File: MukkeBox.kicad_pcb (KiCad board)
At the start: 2 copper layers, 200 x 105 mm, 278 parts, among them J101 Conn_02x20_Odd_Even, J102 Conn_01x04, J103 Conn_02x05_Odd_Even, J104 Conn_02x05_Odd_Even, J301 Conn_02x04_Odd_Even, J302 Conn_02x04_Odd_Even, J303 TB001-500-04BE CUI_Devices, J401 TB001-500-02BE CUI_Devices, J501 TB001-500-04BE CUI_Devices, J601 Conn_01x03_Female, J602 Conn_02x01, J603 Conn_02x06_Odd_Even, J604 Conn_02x01, J605 Conn_02x01, Q1 2N7002, Q201 VS6412AE, Q301 2N7002, Q302 HSBB3103, Q303 2N7002, Q304 HSBB3103, Q305 VS6412AE, Q306 2N7002, Q307 BSS84, Q308 2N7002, Q309 VS6412AE, Q310 HSBB3103, Q311 HSBB3103, Q501 2N7002, SW501 DS04-254-2-02BK-SMT, U101 LM35-LP, U102 STM32F030C6Tx_MukkeBox, U103 MCP9700, U202 StepUp, U203 TPS40210, U301 BQ24610, U501 TDA7498L, U502 BK8000L, U503 TDA7719, U504 AP2553AW6-7, U505 JW5026, U602 JW5026, Y101 FOXSDLF/080-20

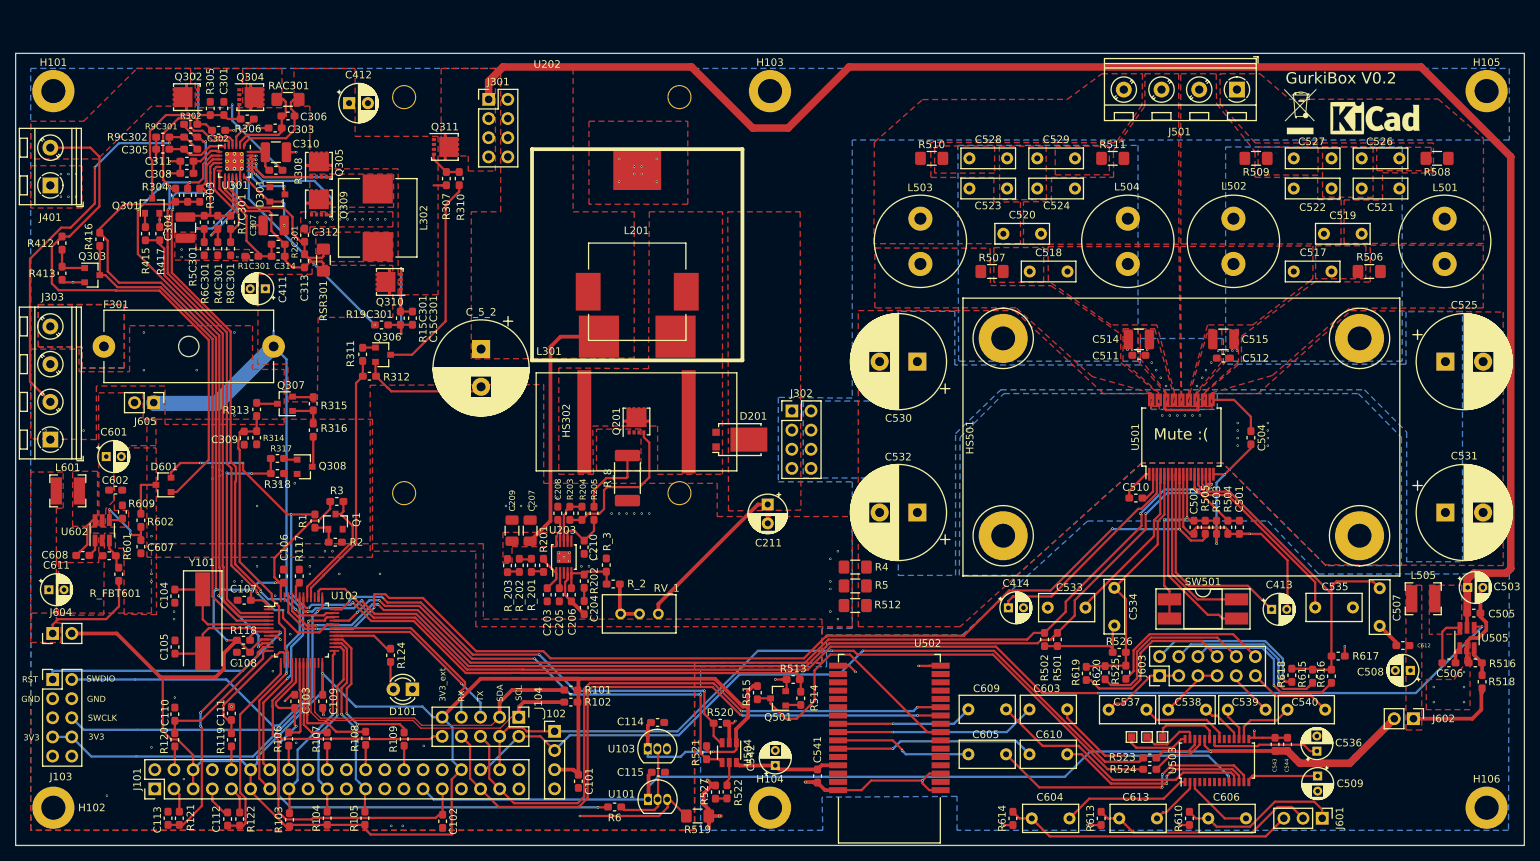
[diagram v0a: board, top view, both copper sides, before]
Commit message: Fehler bei Bestellung behoben: größere Vias. Platinen erfolgreich erhalten
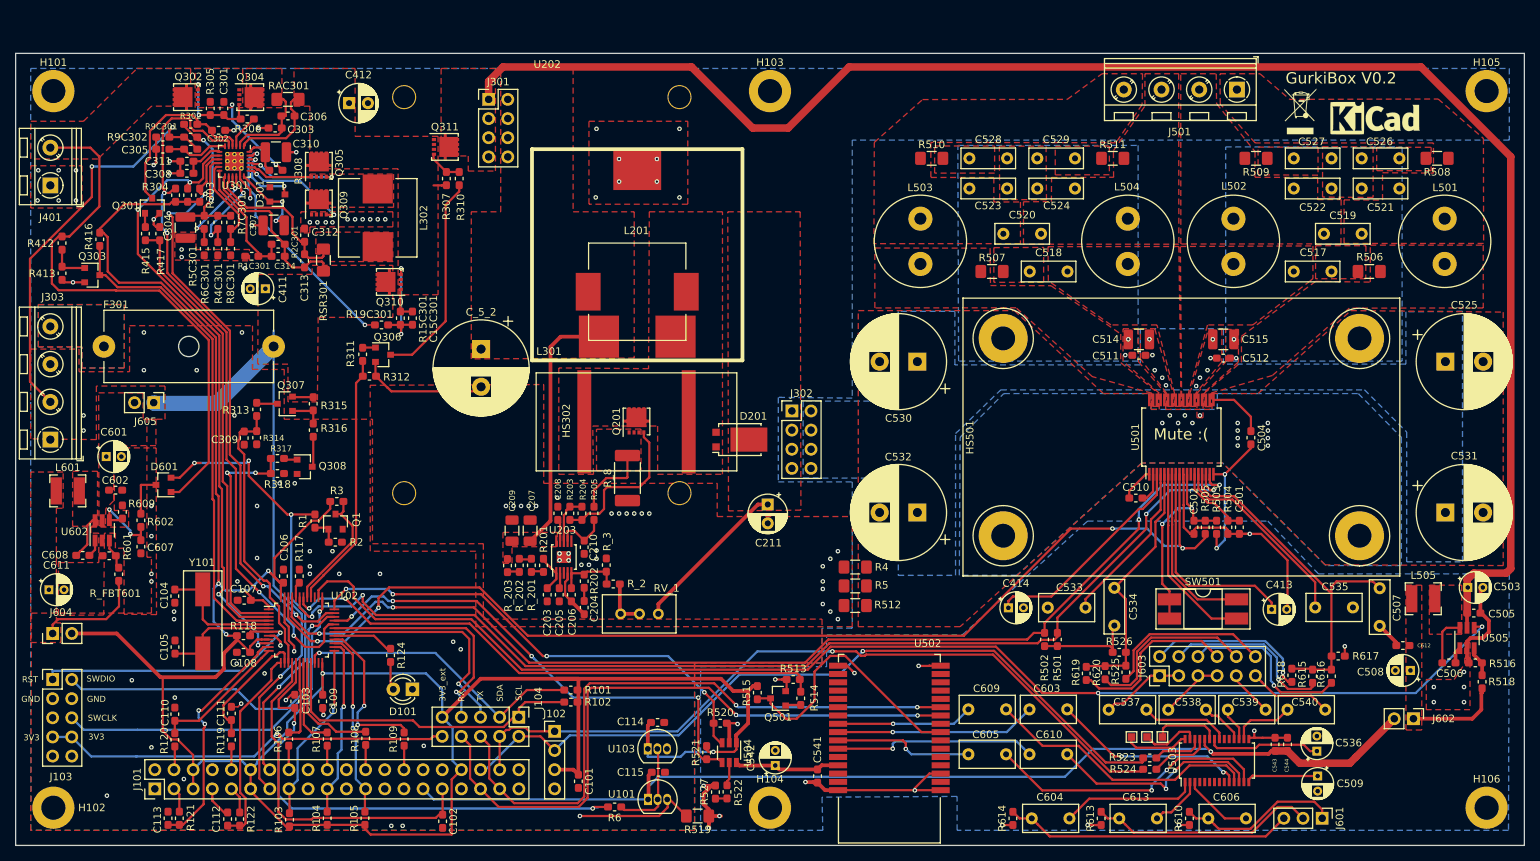
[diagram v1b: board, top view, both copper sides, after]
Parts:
- moved R118 0.60 mm to (75.7, 114.3)
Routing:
- net GND: track 61.8 -> 75.4 mm
- net GNDPWR: track 7.14 -> 0.00 mm, vias 20 -> 18
- net /UART1_RX: track 25.3 -> 31.2 mm
- net /UART1_TX: track 25.2 -> 30.4 mm
- net /I2C1_SDA: track 43.5 -> 39.2 mm, vias 0 -> 1
- net STBY_TDA7498: track 142.1 -> 146.3 mm
- net CHARGER_STAT1: track 92.5 -> 96.3 mm
- net +3V3: track 351.1 -> 354.5 mm
- net DIAG_TDA7498: track 146.6 -> 150.0 mm
- net /SWDIO: track 49.3 -> 46.0 mm
- net MUTE_TDA7498: track 140.8 -> 144.0 mm
- net Net-(C610-Pad2): track 27.0 -> 28.6 mm
- net /00_Charger/VREF: track 25.0 -> 26.6 mm
- net /00_Charger/TS: track 53.2 -> 54.7 mm
- net 3V3_EN: track 60.7 -> 62.2 mm
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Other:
- net class Default: trace_width 0.15 -> 0.2; via_dia 0.3 -> 0.6; via_drill 0.2 -> 0.3
- rule trace_min: 0.15 -> 0.2
- rule via_min_drill: 0.2 -> 0.3
- rule via_min_size: 0.3 -> 0.6

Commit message: Bereit zur Bestellung
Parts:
- removed C102, C115, C501, C502, C504, C510, C511: 100n, Capacitor_SMD:C_0603_1608Metric_Pad1.05x0.95mm_HandSolder
- removed C413, C414: 10u, Capacitor_THT:CP_Radial_D4.0mm_P2.00mm
- removed C514, C515: 2.2u, Capacitor_SMD:C_1210_3225Metric
- removed C517, C518: 1n, Capacitor_THT:C_Rect_L7.0mm_W2.5mm_P5.00mm
- removed C519: 470n, Capacitor_THT:C_Rect_L7.0mm_W2.5mm_P5.00mm
- removed C521, C522, C523, C524, C526, C527: 220n, Capacitor_THT:C_Rect_L7.0mm_W2.5mm_P5.00mm
- removed C531, C532: 560u 50V, Capacitor_THT:CP_Radial_D12.5mm_P5.00mm
- removed J501: TB001-500-04BE CUI_Devices, TerminalBlock_RND:TerminalBlock_RND_205-00047_1x04_P5.00mm_Horizontal
- removed L501, L502, L504: 22uH 6100-220K-RC, Inductor_THT:L_Radial_D12.0mm_P6.00mm_MuRATA_1900R
- removed R108: 1K, Resistor_SMD:R_0603_1608Metric_Pad1.05x0.95mm_HandSolder
- removed R501, R502: 100K, Resistor_SMD:R_0603_1608Metric_Pad1.05x0.95mm_HandSolder
- removed R503: 22R, Resistor_SMD:R_0603_1608Metric_Pad1.05x0.95mm_HandSolder
- removed R504: 39K, Resistor_SMD:R_0603_1608Metric_Pad1.05x0.95mm_HandSolder
- removed R506, R507: 22R, Resistor_SMD:R_1206_3216Metric_Pad1.42x1.75mm_HandSolder
- removed R508, R509: 8R, Resistor_SMD:R_1206_3216Metric_Pad1.42x1.75mm_HandSolder
- removed REF**: WEEE-Logo_4.2x6mm_SilkScreen, Symbol:WEEE-Logo_4.2x6mm_SilkScreen
- removed REF**: KiCAD Logo, Symbol:Symbol_KiCAD-Logo_CopperAndSilkScreenTop
- removed SW501: DS04-254-2-02BK-SMT, Package_DIP:DIP-4_W8.89mm_SMDSocket_LongPads
- removed TP502: TestPoint, TestPoint:TestPoint_Pad_1.0x1.0mm
- removed U101: LM35-LP, Package_TO_SOT_THT:TO-92_Inline
- removed U501: TDA7498L, Package_SO:ST_PowerSSO-36_TDA7498
- added C1: 1n, Capacitor_THT:C_Rect_L7.0mm_W2.5mm_P5.00mm, F.Cu at (196.3, 108.3)
- added C10: 100n, Capacitor_SMD:C_0603_1608Metric_Pad1.05x0.95mm_HandSolder, F.Cu at (203.6, 83.2)
- added C11: 220n, Capacitor_SMD:C_0603_1608Metric_Pad1.05x0.95mm_HandSolder, F.Cu at (202.7, 76.7)
- added C12: 220n, Capacitor_SMD:C_0603_1608Metric_Pad1.05x0.95mm_HandSolder, F.Cu at (208.5, 76.7)
- added C13: 220n, Capacitor_SMD:C_0603_1608Metric_Pad1.05x0.95mm_HandSolder, F.Cu at (211.8, 76.7)
- added C14: 220n, Capacitor_SMD:C_0603_1608Metric_Pad1.05x0.95mm_HandSolder, F.Cu at (217.2, 76.7)
- added C15: 1u, Capacitor_SMD:C_1210_3225Metric_Pad1.42x2.65mm_HandSolder, F.Cu at (173.5, 54.5)
- added C16: 1u, Capacitor_SMD:C_1210_3225Metric_Pad1.42x2.65mm_HandSolder, F.Cu at (181.7, 54.5)
- added C17: 1u, Capacitor_SMD:C_1210_3225Metric_Pad1.42x2.65mm_HandSolder, F.Cu at (195.9, 54.6)
- added C18: 1u, Capacitor_SMD:C_1210_3225Metric_Pad1.42x2.65mm_HandSolder, F.Cu at (204.1, 54.5)
- added C19: 1u, Capacitor_SMD:C_1210_3225Metric_Pad1.42x2.65mm_HandSolder, F.Cu at (226.4, 54.5)
- added C2: 1u, Capacitor_THT:C_Rect_L7.2mm_W3.5mm_P5.00mm_FKS2_FKP2_MKS2_MKP2, F.Cu at (200.5, 110.7)
- added C24: 10n, Capacitor_SMD:C_1210_3225Metric_Pad1.42x2.65mm_HandSolder, F.Cu at (176.2, 48.8)
- added C25: 10n, Capacitor_SMD:C_1210_3225Metric_Pad1.42x2.65mm_HandSolder, F.Cu at (181.1, 48.8)
- added C26: 10n, Capacitor_SMD:C_1210_3225Metric_Pad1.42x2.65mm_HandSolder, F.Cu at (197.8, 49.0)
- added C27: 10n, Capacitor_SMD:C_1210_3225Metric_Pad1.42x2.65mm_HandSolder, F.Cu at (202.7, 49.0)
- added C3: 1n, Capacitor_SMD:C_0603_1608Metric_Pad1.05x0.95mm_HandSolder, F.Cu at (218.7, 90.4)
- added C315: 100n, Capacitor_SMD:C_0603_1608Metric_Pad1.05x0.95mm_HandSolder, F.Cu at (82.8, 56.3)
- added C4: 100n, Capacitor_SMD:C_0603_1608Metric_Pad1.05x0.95mm_HandSolder, F.Cu at (217.8, 83.2)
- added C401: 1u, Capacitor_SMD:C_0603_1608Metric_Pad1.05x0.95mm_HandSolder, F.Cu at (210.7, 95.7)
- added C402: 1u, Capacitor_SMD:C_0603_1608Metric_Pad1.05x0.95mm_HandSolder, F.Cu at (188.8, 95.0)
- added C403: 560u 50V, Capacitor_THT:CP_Radial_D12.5mm_P5.00mm, F.Cu at (235.1, 98.0)
- added C404: 560u 50V, Capacitor_THT:CP_Radial_D12.5mm_P5.00mm, F.Cu at (165.0, 98.1)
- added C405: 1n, Capacitor_SMD:C_0603_1608Metric_Pad1.05x0.95mm_HandSolder, F.Cu at (219.3, 83.2)
- added C406: 1n, Capacitor_SMD:C_0603_1608Metric_Pad1.05x0.95mm_HandSolder, F.Cu at (198.0, 83.3)
- added C407: 1n, Capacitor_SMD:C_0603_1608Metric_Pad1.05x0.95mm_HandSolder, F.Cu at (180.7, 83.2)
- added C408: 1n, Capacitor_SMD:C_0603_1608Metric_Pad1.05x0.95mm_HandSolder, F.Cu at (202.1, 83.2)
- added C5: 100n, Capacitor_SMD:C_0603_1608Metric_Pad1.05x0.95mm_HandSolder, F.Cu at (196.5, 83.3)
- added C6: 220n, Capacitor_SMD:C_0603_1608Metric_Pad1.05x0.95mm_HandSolder, F.Cu at (182.3, 76.7)
- added C7: 220n, Capacitor_SMD:C_0603_1608Metric_Pad1.05x0.95mm_HandSolder, F.Cu at (187.9, 76.8)
- added C8: 220n, Capacitor_SMD:C_0603_1608Metric_Pad1.05x0.95mm_HandSolder, F.Cu at (191.2, 76.8)
- added C9: 220n, Capacitor_SMD:C_0603_1608Metric_Pad1.05x0.95mm_HandSolder, F.Cu at (197.1, 76.8)
- added J1: TB001-500-06BE CUI_Devices, TerminalBlock_RND:TerminalBlock_RND_205-00049_1x06_P5.00mm_Horizontal, F.Cu at (185.0, 41.7)
- added L1: MMD-10DZ-100M-X2, Inductor_SMD:L_Wuerth_HCI-1030, F.Cu at (172.1, 62.8)
- added L2: MMD-10DZ-100M-X2, Inductor_SMD:L_Wuerth_HCI-1030, F.Cu at (183.3, 62.8)
- added L3: MMD-10DZ-100M-X2, Inductor_SMD:L_Wuerth_HCI-1030, F.Cu at (194.5, 62.8)
- added L4: MMD-10DZ-100M-X2, Inductor_SMD:L_Wuerth_HCI-1030, F.Cu at (205.7, 62.8)
- added L5: MMD-10DZ-100M-X2, Inductor_SMD:L_Wuerth_HCI-1030, F.Cu at (228.1, 62.8)
- added R10: 100K, Resistor_SMD:R_0603_1608Metric_Pad1.05x0.95mm_HandSolder, F.Cu at (91.2, 117.2)
- added R11: 100K, Resistor_SMD:R_0603_1608Metric_Pad1.05x0.95mm_HandSolder, F.Cu at (82.8, 102.4)
- added R110: 100K, Resistor_SMD:R_0603_1608Metric_Pad1.05x0.95mm_HandSolder, F.Cu at (85.8, 130.9)
- added R111: 100K, Resistor_SMD:R_0603_1608Metric_Pad1.05x0.95mm_HandSolder, F.Cu at (88.7, 130.9)
- added R12: 100K, Resistor_SMD:R_0603_1608Metric_Pad1.05x0.95mm_HandSolder, F.Cu at (187.9, 92.5)
- added R13: 20K, Resistor_SMD:R_0603_1608Metric_Pad1.05x0.95mm_HandSolder, F.Cu at (189.7, 92.5)
- added R14: 100K, Resistor_SMD:R_0603_1608Metric_Pad1.05x0.95mm_HandSolder, F.Cu at (182.5, 91.4)
- added R15: 10K, Resistor_SMD:R_0603_1608Metric_Pad1.05x0.95mm_HandSolder, F.Cu at (200.0, 88.6)
- added R16: 3.3R, Resistor_SMD:R_1210_3225Metric_Pad1.42x2.65mm_HandSolder, F.Cu at (171.2, 48.8)
- added R17: 3.3R, Resistor_SMD:R_1210_3225Metric_Pad1.42x2.65mm_HandSolder, F.Cu at (185.9, 48.8)
- added R18: 3.3R, Resistor_SMD:R_1210_3225Metric_Pad1.42x2.65mm_HandSolder, F.Cu at (192.8, 49.0)
- added R19: 3.3R, Resistor_SMD:R_1210_3225Metric_Pad1.42x2.65mm_HandSolder, F.Cu at (207.5, 49.0)
- added R20: DNP, Resistor_SMD:R_0603_1608Metric_Pad1.05x0.95mm_HandSolder, F.Cu at (215.2, 115.2)
- added R21: 100K, Resistor_SMD:R_0603_1608Metric_Pad1.05x0.95mm_HandSolder, F.Cu at (205.2, 92.4)
- added R401: DNP, Resistor_SMD:R_0603_1608Metric_Pad1.05x0.95mm_HandSolder, F.Cu at (209.1, 98.0)
- added R402: DNP, Resistor_SMD:R_0603_1608Metric_Pad1.05x0.95mm_HandSolder, F.Cu at (187.3, 96.7)
- added R403: 10K, Resistor_SMD:R_0603_1608Metric_Pad1.05x0.95mm_HandSolder, F.Cu at (208.2, 95.6)
- added R404: 10K, Resistor_SMD:R_0603_1608Metric_Pad1.05x0.95mm_HandSolder, F.Cu at (186.4, 94.2)
- added R7: 100K, Resistor_SMD:R_0603_1608Metric_Pad1.05x0.95mm_HandSolder, F.Cu at (193.1, 91.6)
- added R8: 47K, Resistor_SMD:R_0603_1608Metric_Pad1.05x0.95mm_HandSolder, F.Cu at (209.9, 93.3)
- added R9: 75K, Resistor_SMD:R_0603_1608Metric_Pad1.05x0.95mm_HandSolder, F.Cu at (211.4, 93.3)
- added U1: TPA3116D2, MukkeBox:HTSSOP-32-TPA3116D2, F.Cu at (210.6, 85.0)
- added U2: TPA3116D2, MukkeBox:HTSSOP-32-TPA3116D2, F.Cu at (189.4, 85.0)
- C110, C111, C112, C113: value 10n -> 100n
- C205: value 100n -> 1u
- C411, C503, C508, C509, C536, C542, C601, C611: footprint Capacitor_THT:CP_Radial_D4.0mm_P2.00mm -> Capacitor_SMD:C_1206_3216Metric_Pad1.42x1.75mm_HandSolder
- C520: value 470n -> 1u; footprint Capacitor_THT:C_Rect_L7.0mm_W2.5mm_P5.00mm -> Capacitor_SMD:C_1210_3225Metric_Pad1.42x2.65mm_HandSolder
- C528, C529: value 220n -> 10n; footprint Capacitor_THT:C_Rect_L7.0mm_W2.5mm_P5.00mm -> Capacitor_SMD:C_1210_3225Metric_Pad1.42x2.65mm_HandSolder
- J104: value Conn_02x05_Odd_Even -> Conn_02x01; footprint Connector_PinHeader_2.54mm:PinHeader_2x05_P2.54mm_Vertical -> Connector_PinHeader_2.54mm:PinHeader_1x02_P2.54mm_Vertical
- L503: value 22uH 6100-220K-RC -> MMD-10DZ-100M-X2; footprint Inductor_THT:L_Radial_D12.0mm_P6.00mm_MuRATA_1900R -> Inductor_SMD:L_Wuerth_HCI-1030
- R104, R105, R309: value 100K -> 1K
- R109: value 1K -> 100K
- R510, R511: value 8R -> 3.3R; footprint Resistor_SMD:R_1206_3216Metric_Pad1.42x1.75mm_HandSolder -> Resistor_SMD:R_1210_3225Metric_Pad1.42x2.65mm_HandSolder
- R513, R520, R521: value 10K -> 100K
- R514: value 100R -> 1K
- R523, R524: value 47R -> 100R
- R9C301: value 2K2 -> 10K
- R9C302: value 6K8 -> 470K
- R_3: value 422R -> 1K5
- moved J104 59.9 mm to (52.9, 116.5)
- moved L503 51.5 mm to (216.9, 62.8)
- moved R510 48.3 mm to (215.1, 48.8)
- moved C528 48.2 mm to (220.1, 48.8)
- moved C529 44.1 mm to (225.0, 48.8)
- moved C507 43.2 mm to (183.1, 113.4)
- moved C520 42.4 mm to (218.3, 54.5)
- moved R511 39.0 mm to (229.8, 48.8)
- moved R617 34.1 mm to (186.8, 114.0), turned to 0 degrees
- moved C533 32.6 mm to (219.9, 110.6)
- moved R526 31.2 mm to (222.9, 115.2), turned to 180 degrees
- moved R616 30.7 mm to (189.2, 118.1)
- moved C535 30.4 mm to (192.4, 110.6)
- moved R619 30.4 mm to (217.6, 116.1)
- moved R615 29.7 mm to (187.7, 118.1)
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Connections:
- net /Amplifier/SPEAKER_R+ renamed /Amplifier/SUB+
- C103 pad 1: /TEMP_SENSOR2 -> /TEMP_SENSOR1
- C110 pad 1: GND -> /MIDDLE
- C110 pad 2: /BASS -> GND
- C111 pad 1: /TREBLE -> GND
- C111 pad 2: GND -> /TREBLE
- C112 pad 1: GND -> /GAIN
- C112 pad 2: /MIDDLE -> GND
- C113 pad 1: GND -> /BASS
- C113 pad 2: /GAIN -> GND
- C509 pad 1: Net-(C509-Pad1) -> GNDA
- C509 pad 2: GNDA -> Net-(C509-Pad2)
- C520 pad 2: /Amplifier/SPEAKER_R- -> GNDPWR
- C534 pad 1: TO_SPEAKER_R -> TO_SUB
- J101 pad 10: Net-(J101-Pad10) -> GND
- J101 pad 11: +3V3 -> Net-(J101-Pad11)
- J101 pad 15: /INPUT1 -> Net-(J101-Pad15)
- J101 pad 16: Net-(J101-Pad16) -> GND
- J101 pad 17: GND -> Net-(J101-Pad17)
- J101 pad 19: /INPUT2 -> Net-(J101-Pad19)
- J101 pad 2: GND -> Net-(J101-Pad2)
- J101 pad 20: Net-(J101-Pad20) -> GND
- J101 pad 21: GND -> Net-(J101-Pad21)
- J101 pad 23: /INPUT3 -> GND
- J101 pad 24: Net-(J101-Pad24) -> +3V3
- J101 pad 26: GND -> +3V3
- J101 pad 27: Net-(J101-Pad27) -> GND
- J101 pad 28: Net-(J101-Pad28) -> +3V3
- J101 pad 29: +8V -> GND
- J101 pad 3: Net-(J101-Pad3) -> +3V3
- J101 pad 30: GND -> +3V3
- J101 pad 31: /TEMP_SENSOR1 -> GND
- J101 pad 32: Net-(J101-Pad32) -> +3V3
- J101 pad 34: +3V3 -> RxT
- J101 pad 35: RxT -> TxR
- J101 pad 36: SCL -> GND
- J101 pad 37: TxR -> +3V3
- J101 pad 38: SDA -> SCL
- J101 pad 39: GND -> SDA
- J101 pad 4: Net-(J101-Pad4) -> GND
- J101 pad 5: +3V3 -> Net-(J101-Pad5)
- J101 pad 8: GND -> Net-(J101-Pad8)
- J101 pad 9: Net-(J101-Pad9) -> +3V3
- J104 pad 1: /I2C1_SCL -> +3V3
- J104 pad 2: SCL -> /ST_Link_3V3
- J603 pad 3: Net-(C537-Pad1) -> Net-(C538-Pad1)
- J603 pad 5: Net-(C538-Pad1) -> Net-(C537-Pad1)
- R101 pad 1: /I2C1_SDA -> SDA
- R102 pad 1: /I2C1_SCL -> SCL
- R103 pad 2: /INPUT1 -> /GPIO1
- R104 pad 1: +3V3 -> /GPIO1
- R104 pad 2: /INPUT2 -> Net-(J101-Pad15)
- R105 pad 1: +3V3 -> /GPIO2
- R105 pad 2: /INPUT3 -> Net-(J101-Pad17)
- R106 pad 1: Net-(J101-Pad16) -> /GPIO3
- R106 pad 2: /OUTPUT1 -> Net-(J101-Pad19)
- R107 pad 1: Net-(J101-Pad20) -> /GPIO4
- R107 pad 2: /OUTPUT2 -> Net-(J101-Pad21)
- R109 pad 1: Net-(J101-Pad28) -> +3V3
- R109 pad 2: /OUTPUT4 -> /GPIO2
- R119 pad 1: Net-(J101-Pad10) -> /TREBLE
- R119 pad 2: /TREBLE -> Net-(J101-Pad11)
- R120 pad 1: Net-(J101-Pad4) -> /BASS
- R120 pad 2: /BASS -> Net-(J101-Pad5)
- R121 pad 1: Net-(J101-Pad3) -> /GAIN
- R121 pad 2: /GAIN -> Net-(J101-Pad2)
- R122 pad 1: Net-(J101-Pad9) -> /MIDDLE
- R122 pad 2: /MIDDLE -> Net-(J101-Pad8)
- R505 pad 1: DIAG_TDA7498 -> MUTE_AMP2
- R505 pad 2: /Amplifier/VDDS -> GNDA
- R511 pad 2: /Amplifier/SPEAKER_R- -> /Amplifier/SUB-
- R525 pad 1: TO_SPEAKER_R -> TO_SUB
- R526 pad 2: TO_SPEAKER_R -> TO_SUB
- R6 pad 2: /TEMP_SENSOR2 -> /TEMP_SENSOR1
- R616 pad 1: TO_SPEAKER_L -> TO_SPEAKER_R
- R620 pad 1: TO_SPEAKER_R -> TO_SUB
- U102 pad 17: /TEMP_SENSOR2 -> LEVELMETER
- U102 pad 18: /OUTPUT1 -> /GPIO1
- U102 pad 19: /OUTPUT2 -> /GPIO2
- U102 pad 20: /OUTPUT3 -> /GPIO3
- U102 pad 21: /I2C1_SCL -> SCL
- U102 pad 22: /I2C1_SDA -> SDA
- U102 pad 25: /INPUT1 -> /GPIO4
- U102 pad 26: /INPUT2 -> MUTE_AMP2
- U102 pad 27: /INPUT3 -> DIAG_AMP2
- U102 pad 28: /OUTPUT4 -> STEPUP_DISABLE
- U102 pad 30: /UART1_TX -> TxR
- U102 pad 31: /UART1_RX -> RxT
- U102 pad 39: Net-(U102-Pad39) -> STBY_AMP2
- U102 pad 43: MUTE_TDA7498 -> MUTE_AMP1
- U102 pad 45: STBY_TDA7498 -> STBY_AMP1
- U102 pad 46: DIAG_TDA7498 -> DIAG_AMP1
- U203 pad 3: Net-(U203-Pad3) -> STEPUP_DISABLE
- U503 pad 14: Net-(C509-Pad1) -> Net-(C509-Pad2)
- U503 pad 27: Net-(TP502-Pad1) -> LEVELMETER
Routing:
- net MUTE_AMP2: track 0.00 -> 150.2 mm, vias 0 -> 4
- net DIAG_TDA7498: track 150.0 -> 0.00 mm, vias 4 -> 0
- net STBY_TDA7498: track 146.3 -> 0.00 mm, vias 4 -> 0
- net MUTE_TDA7498: track 144.0 -> 0.00 mm, vias 4 -> 0
- net DIAG_AMP2: track 0.00 -> 140.0 mm, vias 0 -> 2
- net STBY_AMP2: track 0.00 -> 138.8 mm
- net DIAG_AMP1: track 0.00 -> 132.2 mm, vias 0 -> 2
- net LEVELMETER: track 0.00 -> 131.1 mm, vias 0 -> 2
- net MUTE_AMP1: track 0.00 -> 130.0 mm, vias 0 -> 2
- net STBY_AMP1: track 0.00 -> 128.7 mm, vias 0 -> 2
- net +8V: track 142.4 -> 30.2 mm
- net /TEMP_SENSOR2: track 66.8 -> 0.00 mm, vias 2 -> 0
- net SDA: track 101.6 -> 153.5 mm
- net STEPUP_DISABLE: track 0.00 -> 46.2 mm, vias 0 -> 2
- net SCL: track 102.6 -> 146.0 mm
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- added copper zone on F.Cu, net /Amplifier/LEFT+
- added copper zone on F.Cu, net /Amplifier/LEFT-
- added copper zone on F.Cu, net /Amplifier/RIGHT+
- added copper zone on F.Cu, net /Amplifier/RIGHT-
- added copper zone on F.Cu, net /Amplifier/SUB-
- added copper zone on F.Cu, net Net-(C13-Pad1)
- added copper zone on F.Cu, net Net-(C24-Pad1)
- added copper zone on F.Cu, net Net-(C25-Pad2)
- added copper zone on F.Cu, net Net-(C26-Pad1)
- added copper zone on F.Cu, net Net-(C27-Pad2)
- added copper zone on F.Cu, net Net-(C6-Pad1)
- added copper zone on F.Cu, net Net-(C7-Pad1)
- added copper zone on F.Cu, net Net-(C8-Pad1)
- added copper zone on F.Cu, net Net-(C9-Pad1)
- removed copper zone on F.Cu, net /Amplifier/SPEAKER_L+
- removed copper zone on F.Cu, net /Amplifier/SPEAKER_L-
- removed copper zone on F.Cu, net /Amplifier/SPEAKER_R-
- removed copper zone on F.Cu, net Net-(C517-Pad1)
- removed copper zone on F.Cu, net Net-(C517-Pad2)
- removed copper zone on F.Cu, net Net-(C518-Pad1)
- removed copper zone on F.Cu, net Net-(C518-Pad2)
- removed copper zone on F.Cu, net Net-(C526-Pad1)
- removed copper zone on F.Cu, net Net-(C527-Pad2)
- removed copper zone on F.Cu, net Net-(L501-Pad1)
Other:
- board text added: "+VDC"
- board text added: "GurkiBox V0.3"
- board text removed: "GurkiBox V0.2"

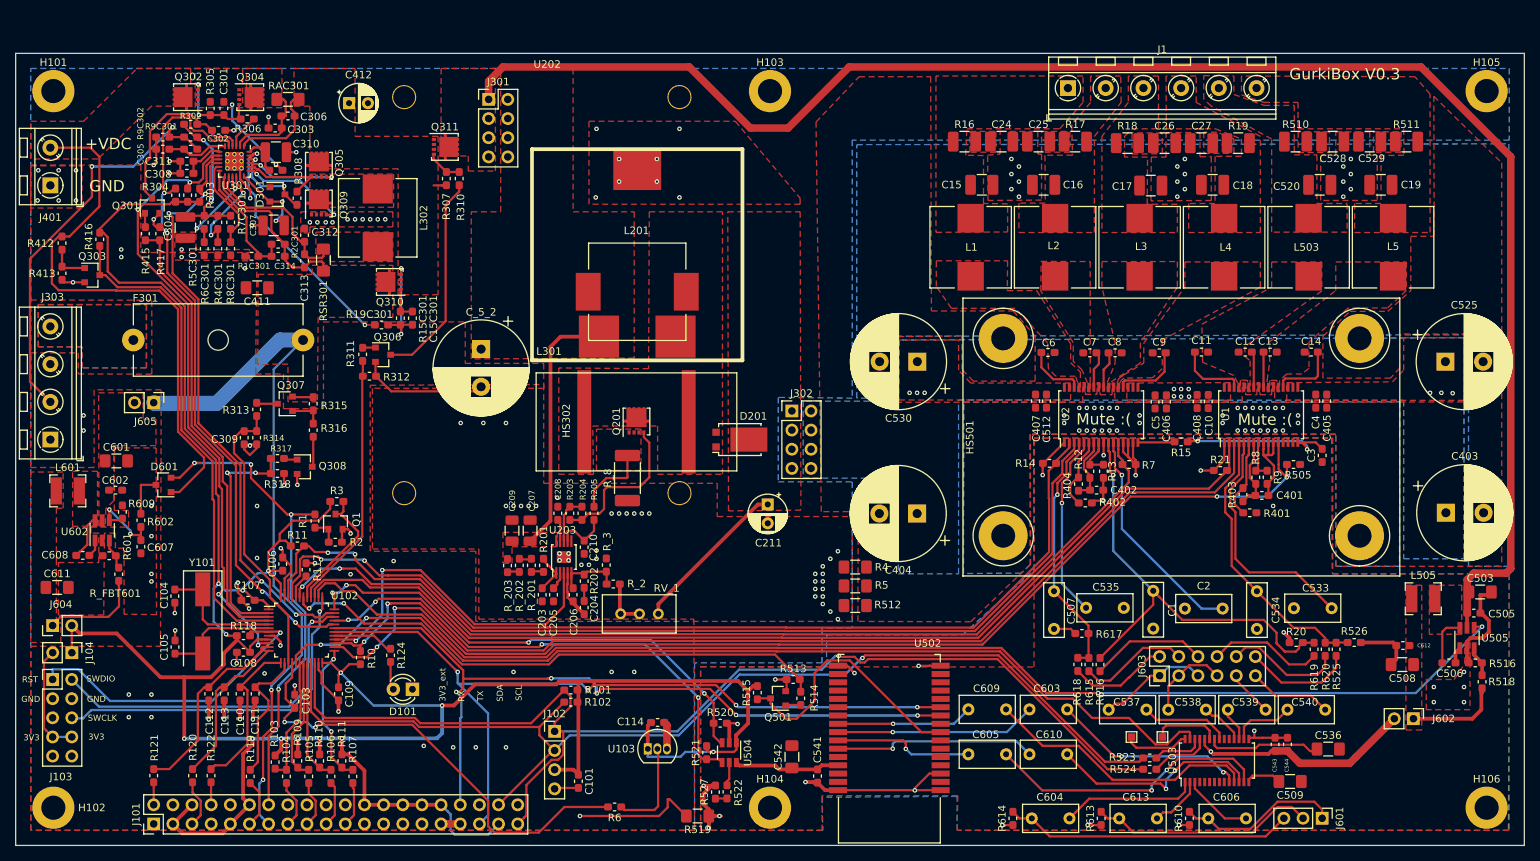
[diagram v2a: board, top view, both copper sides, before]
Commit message: Platine in X um 25mm verkürzt
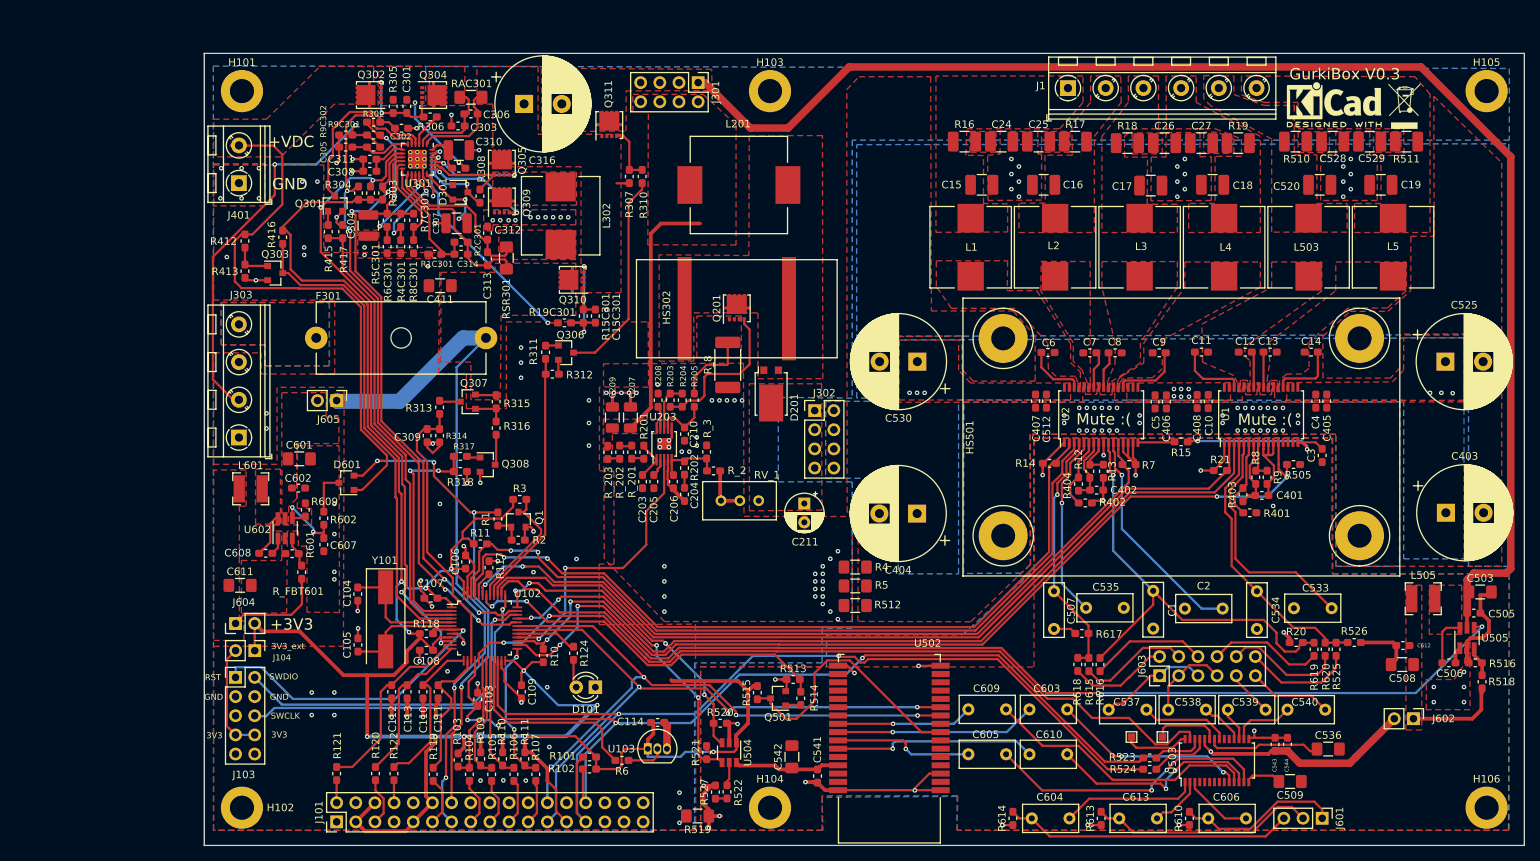
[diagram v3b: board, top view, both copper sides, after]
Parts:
- removed C101: 100n, Capacitor_SMD:C_0603_1608Metric_Pad1.05x0.95mm_HandSolder
- removed C412: 68u, Capacitor_THT:CP_Radial_D5.0mm_P2.50mm
- removed C_5_2: 560u 50V, Capacitor_THT:CP_Radial_D12.5mm_P5.00mm
- removed J102: Conn_01x04, Connector_PinHeader_2.54mm:PinHeader_1x04_P2.54mm_Vertical
- removed L301: 22uH PQ2617BHA-220K, Inductor_SMD:PQ2617BHA-330K
- removed U202: StepUp, Module:StepUpModul
- added C316: 560u 50V, Capacitor_THT:CP_Radial_D12.5mm_P5.00mm, F.Cu at (112.9, 43.8)
- added REF**: WEEE-Logo_4.2x6mm_SilkScreen, Symbol:WEEE-Logo_4.2x6mm_SilkScreen, F.Cu at (229.6, 44.1)
- added REF**: KiCad-Logo2_5mm_SilkScreen, Symbol:KiCad-Logo2_5mm_SilkScreen, F.Cu at (220.3, 43.9)
- J101: footprint Connector_PinHeader_2.54mm:PinHeader_2x20_P2.54mm_Vertical -> Connector_PinHeader_2.54mm:PinHeader_2x17_P2.54mm_Vertical
- moved J301 27.9 mm to (135.9, 41.0), turned to 270 degrees
- moved J401 25.0 mm to (75.1, 54.3)
- moved J303 25.0 mm to (75.1, 88.0)
- moved H101 25.0 mm to (75.5, 42.1)
- moved H102 25.0 mm to (75.5, 137.1)
- moved J101 24.3 mm to (88.0, 139.0)
- moved J605 24.3 mm to (88.0, 83.1)
- moved L601 24.3 mm to (76.6, 94.8)
- moved R121 24.3 mm to (88.0, 132.6)
- moved R_FBT601 24.3 mm to (83.4, 105.9)
- moved C103 24.3 mm to (106.7, 122.7)
- moved C104 24.3 mm to (90.8, 108.8)
- moved C105 24.3 mm to (90.8, 115.5)
- moved C106 24.3 mm to (105.1, 104.5)
- moved C107 24.3 mm to (100.5, 109.3)
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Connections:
- D301 pad 1: Net-(D301-Pad1) -> (no net)
- J101 pad 23: GND -> TxR
- J101 pad 24: +3V3 -> RxT
- J101 pad 25: GND -> +3V3
- J101 pad 26: +3V3 -> GND
- J101 pad 27: GND -> SDA
- J101 pad 28: +3V3 -> SCL
- J101 pad 29: GND -> (no net)
- J101 pad 30: +3V3 -> (no net)
- J101 pad 31: GND -> (no net)
- J101 pad 32: +3V3 -> (no net)
- J101 pad 33: GND -> (no net)
- J101 pad 34: RxT -> (no net)
- J103 pad 10: Net-(J103-Pad10) -> (no net)
- J103 pad 5: Net-(J103-Pad5) -> (no net)
- J103 pad 9: Net-(J103-Pad9) -> (no net)
- U502 pad 12: Net-(U502-Pad12) -> (no net)
- U502 pad 13: Net-(U502-Pad13) -> (no net)
- U502 pad 14: Net-(U502-Pad14) -> (no net)
- U502 pad 15: Net-(U502-Pad15) -> (no net)
- U502 pad 18: Net-(U502-Pad18) -> (no net)
- U502 pad 19: Net-(U502-Pad19) -> (no net)
- U502 pad 2: Net-(U502-Pad2) -> (no net)
- U502 pad 20: Net-(U502-Pad20) -> (no net)
- U502 pad 21: Net-(U502-Pad21) -> (no net)
- U502 pad 22: Net-(U502-Pad22) -> (no net)
- U502 pad 23: Net-(U502-Pad23) -> (no net)
- U502 pad 28: Net-(U502-Pad28) -> (no net)
- U502 pad 30: Net-(U502-Pad30) -> (no net)
- U502 pad 31: Net-(U502-Pad31) -> (no net)
- U502 pad 4: Net-(U502-Pad4) -> (no net)
- U502 pad 5: Net-(U502-Pad5) -> (no net)
- U502 pad 6: Net-(U502-Pad6) -> (no net)
- U502 pad 7: Net-(U502-Pad7) -> (no net)
- U502 pad 9: Net-(U502-Pad9) -> (no net)
- U503 pad 19: Net-(U503-Pad19) -> (no net)
- U503 pad 20: Net-(U503-Pad20) -> (no net)
- U503 pad 4: Net-(U503-Pad4) -> (no net)
- U503 pad 5: Net-(U503-Pad5) -> (no net)
- U503 pad 6: Net-(U503-Pad6) -> (no net)
- U503 pad 7: Net-(U503-Pad7) -> (no net)
- U503 pad 8: Net-(U503-Pad8) -> (no net)
- U503 pad 9: Net-(U503-Pad9) -> (no net)
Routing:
- net +3V3: track 377.4 -> 321.7 mm
- net SYSTEM_LOAD: track 217.7 -> 185.9 mm
- net /TEMP_SENSOR1: track 61.9 -> 32.7 mm
- net SCL: track 146.0 -> 119.9 mm, vias 1 -> 2
- net SDA: track 153.5 -> 129.3 mm, vias 1 -> 2
- net DIAG_AMP1: track 132.2 -> 107.9 mm
- net MUTE_AMP1: track 130.0 -> 105.8 mm
- net STBY_AMP2: track 138.8 -> 114.5 mm
- net DIAG_AMP2: track 140.0 -> 116.0 mm
- net RST_BT: track 74.2 -> 50.1 mm
- net MUTE_AMP2: track 150.2 -> 126.2 mm
- net STBY_AMP1: track 128.7 -> 104.7 mm
- net ENABLE_8V: track 167.4 -> 143.6 mm
- net LEVELMETER: track 131.1 -> 107.3 mm
- net 3V3_BT_FAULT: track 66.3 -> 42.7 mm
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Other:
- board size 200 x 105 mm -> 175 x 105 mm
- board text added: "+3V3"
- board text removed: "RX"
- board text removed: "SCL"
- board text removed: "SDA"
- board text removed: "TX"
